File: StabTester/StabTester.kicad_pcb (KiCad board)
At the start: 2 copper layers, 20 parts

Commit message: added cosmetics
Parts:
- moved H2 71.2 mm to (208.8, 97.6)
- moved H1 71.0 mm to (152.4, 69.1)
- moved H2 71.0 mm to (208.8, 69.1)
- moved MX3 71.0 mm to (152.4, 98.4)
- moved H1 71.0 mm to (152.4, 97.6)
- moved H6 71.0 mm to (165.2, 207.2)
- moved MX3 71.0 mm to (152.4, 69.8)
- moved MX4 71.0 mm to (146.1, 129.4)
- moved MX6 71.0 mm to (148.4, 155.6)
- moved H1 71.0 mm to (111.1, 97.6)
- moved H1 71.0 mm to (111.1, 69.1)
- moved H3 71.0 mm to (146.1, 128.2)
- moved H4 71.0 mm to (148.5, 154.5)
- moved H5 71.0 mm to (155.6, 180.9)
- moved MX1 71.0 mm to (155.6, 181.8)
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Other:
- board outline added: 161.9 x 176.2 mm

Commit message: added graphic
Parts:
- added G***: LOGO, LOGO, F.Cu at (224.6, 142.9)
- moved H4 1.04 mm to (148.4, 155.6)
- moved H5 0.92 mm to (155.6, 181.8)
- moved H6 0.80 mm to (165.1, 208.0)
- moved H1 0.79 mm to (111.1, 98.4)
- moved H1 0.79 mm to (152.4, 98.4)
- moved H2 0.79 mm to (208.8, 98.4)
- moved H1 0.79 mm to (152.4, 69.8)
- moved H1 0.79 mm to (111.1, 69.8)
- moved H2 0.79 mm to (208.8, 69.8)
- moved H3 0.37 mm to (146.1, 128.6)

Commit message: added ruler
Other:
- board size 161.9 x 176.2 mm -> 169.1 x 176.2 mm
- board text added: "0"
- board text added: "1"
- board text added: "2"
- board text added: "3"
- board text added: "4"
- board text added: "5"
- board text added: "6"
- board text added: "7"
- board text added: "8"
- board text added: "U"

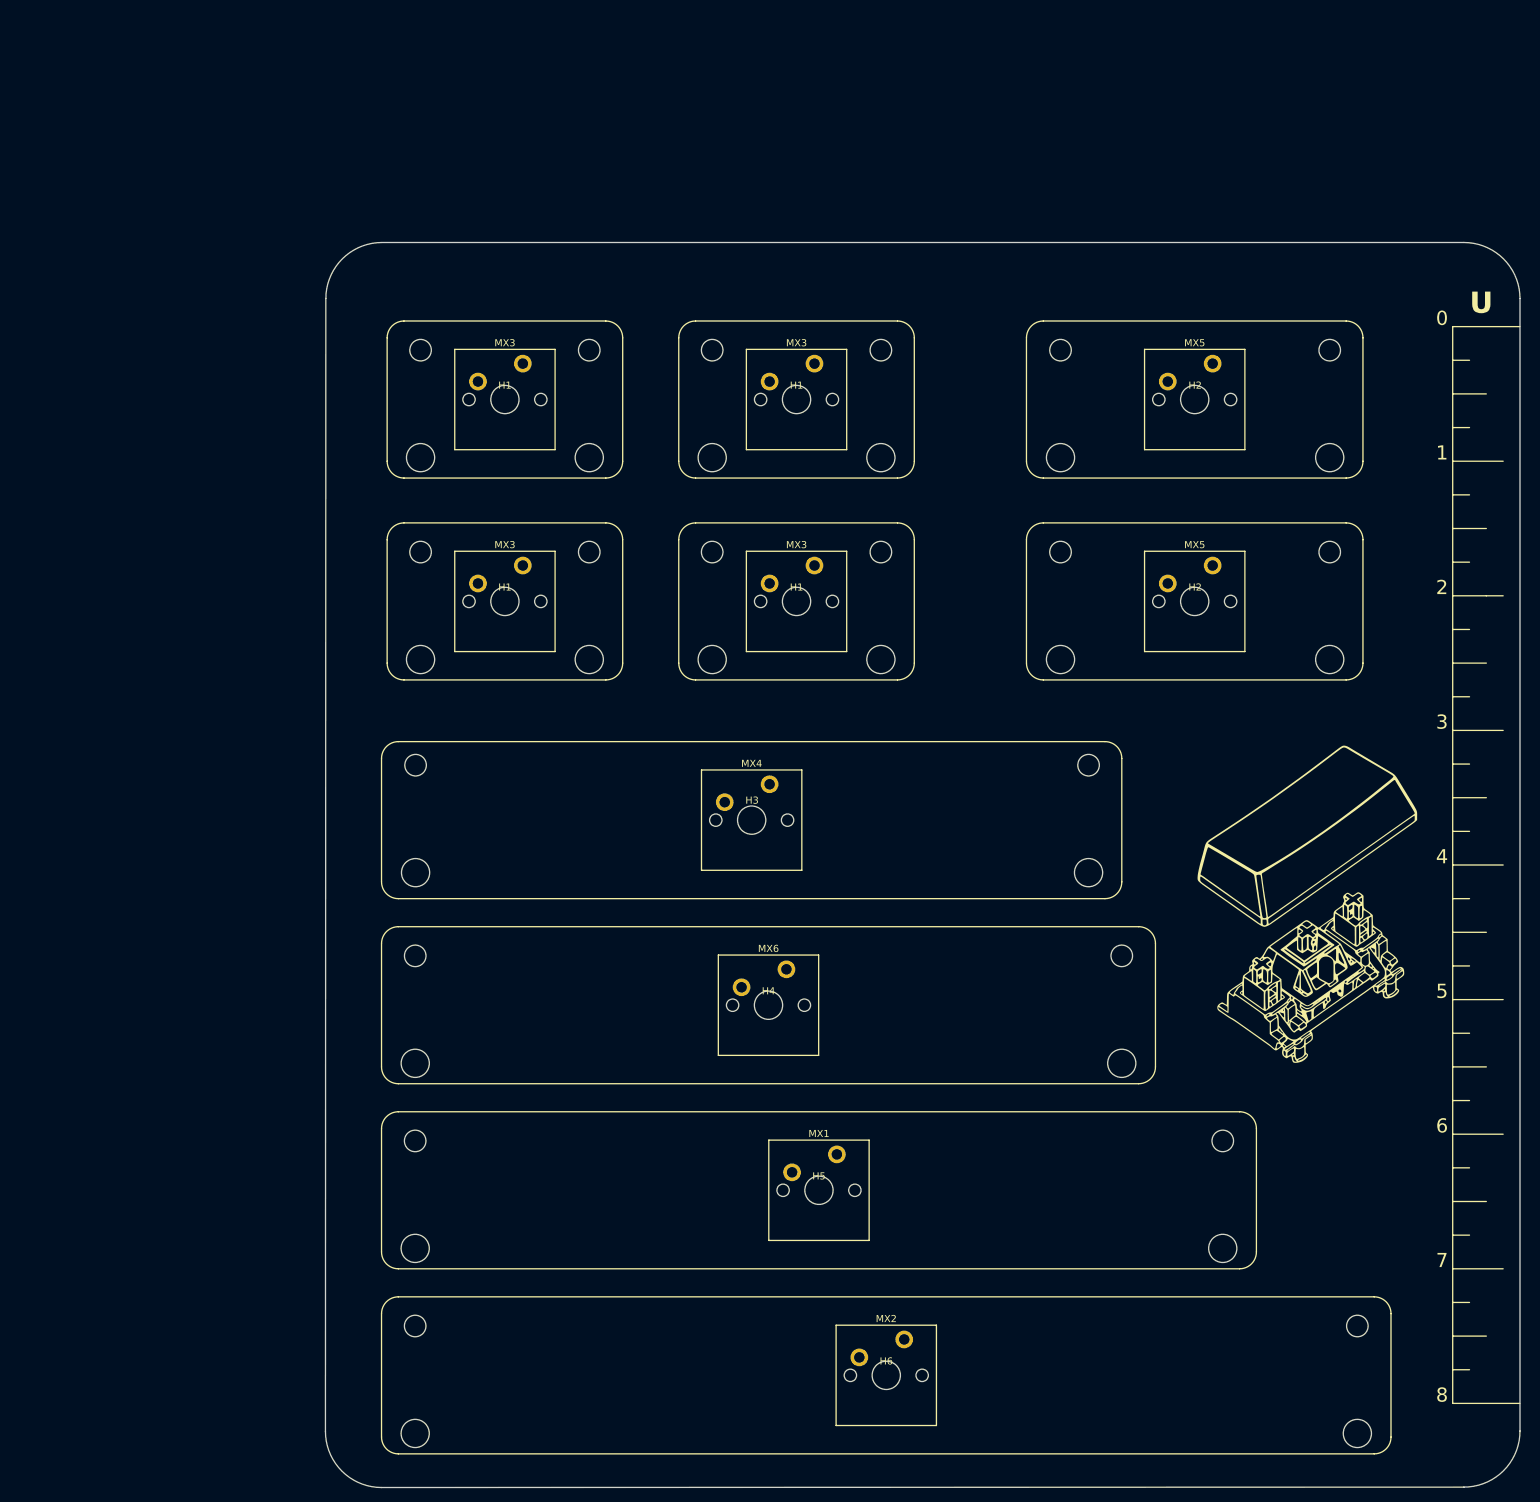
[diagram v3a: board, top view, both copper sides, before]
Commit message: added mounting holes'
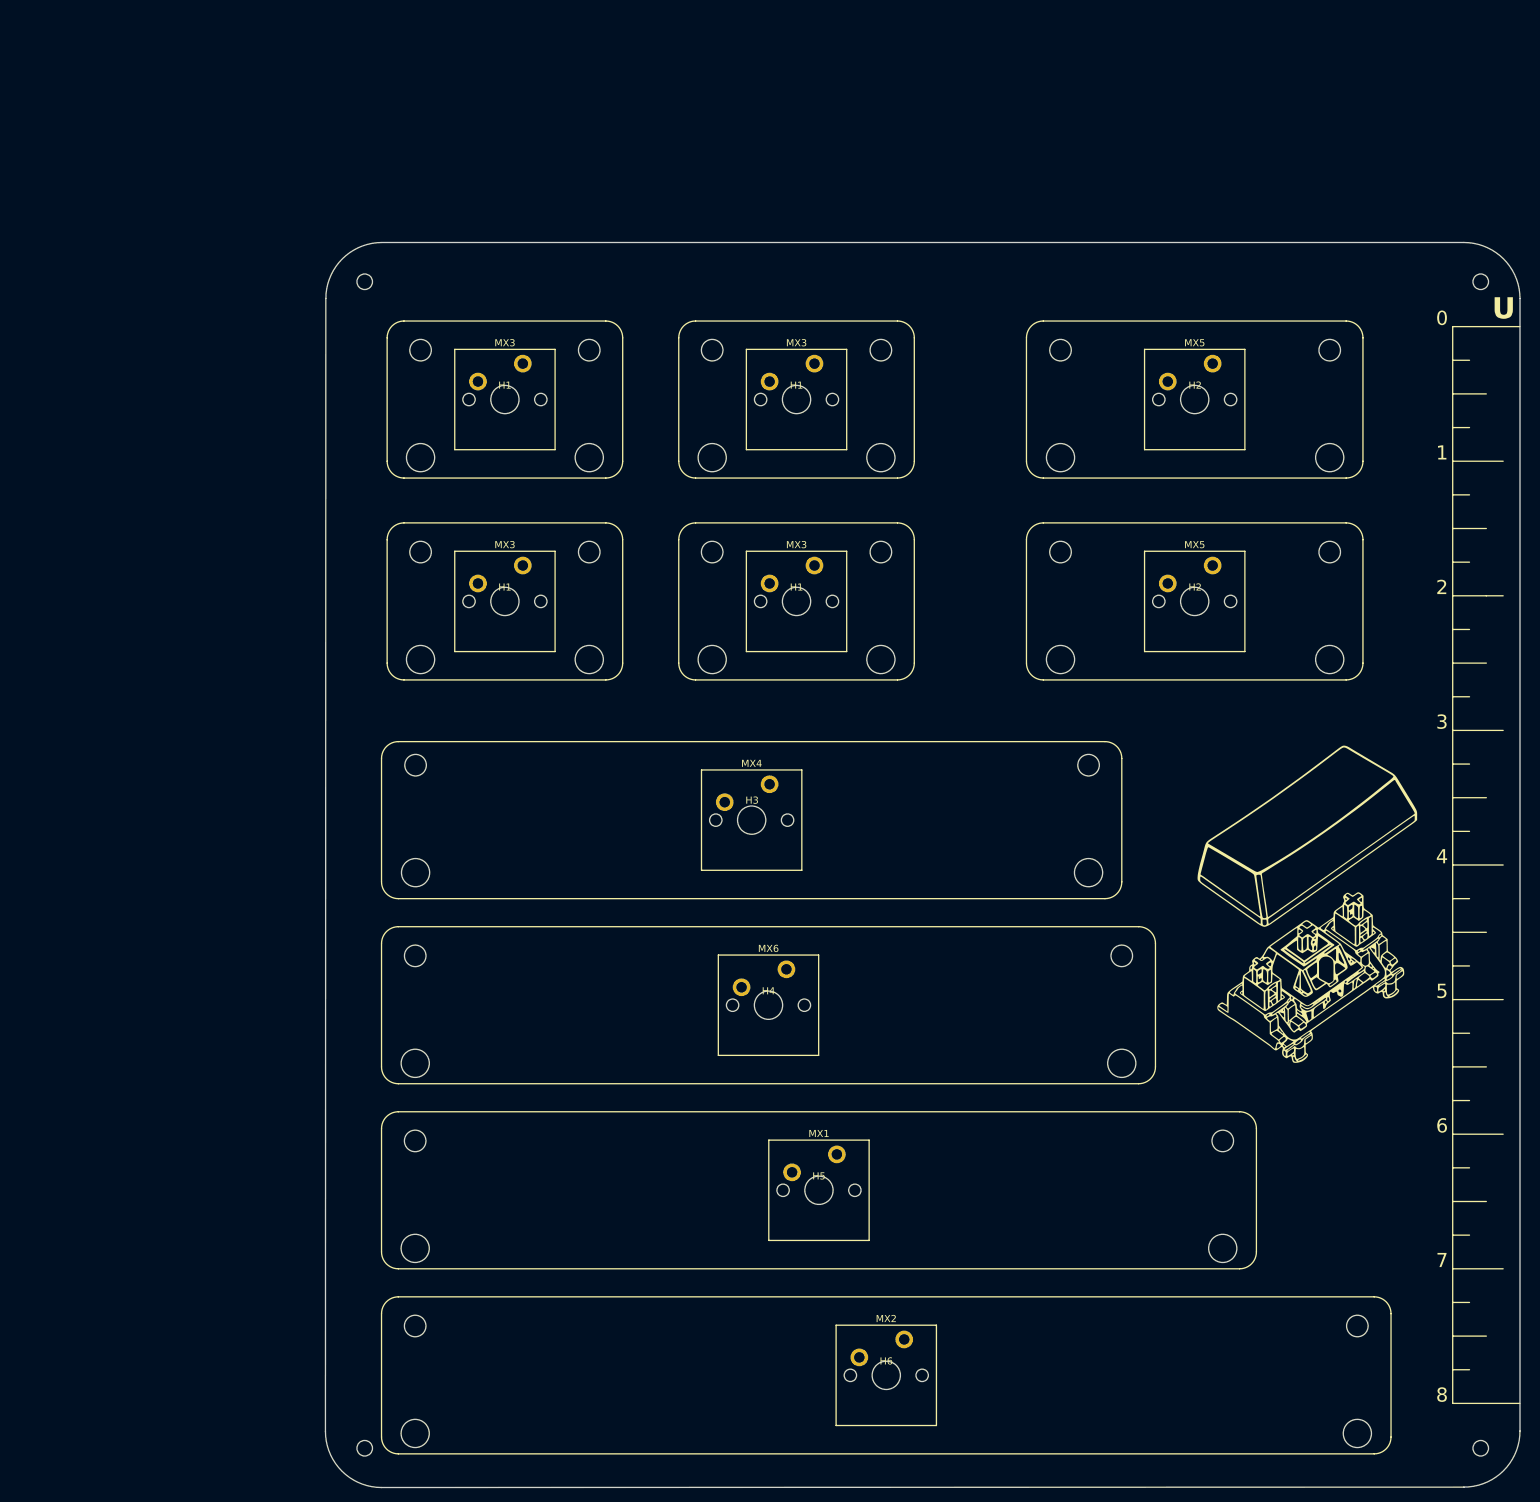
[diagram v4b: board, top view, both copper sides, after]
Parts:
- added H10: MountingHole, MountingHole:MountingHole_2.2mm_M2_ISO7380, F.Cu at (249.2, 53.2)
- added H7: MountingHole, MountingHole:MountingHole_2.2mm_M2_ISO7380, F.Cu at (91.3, 53.2)
- added H8: MountingHole, MountingHole:MountingHole_2.2mm_M2_ISO7380, F.Cu at (91.3, 218.3)
- added H9: MountingHole, MountingHole:MountingHole_2.2mm_M2_ISO7380, F.Cu at (249.2, 218.3)
